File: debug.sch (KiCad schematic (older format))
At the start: 23 parts, among them J102 10118194-0001LF, J401 Conn_01x11, J402 Conn_ARM_JTAG_SWD_10, J403 FTDI_TTL_Cable, SW401 PTS810, U103 CP2102N-A02-GQFN28R

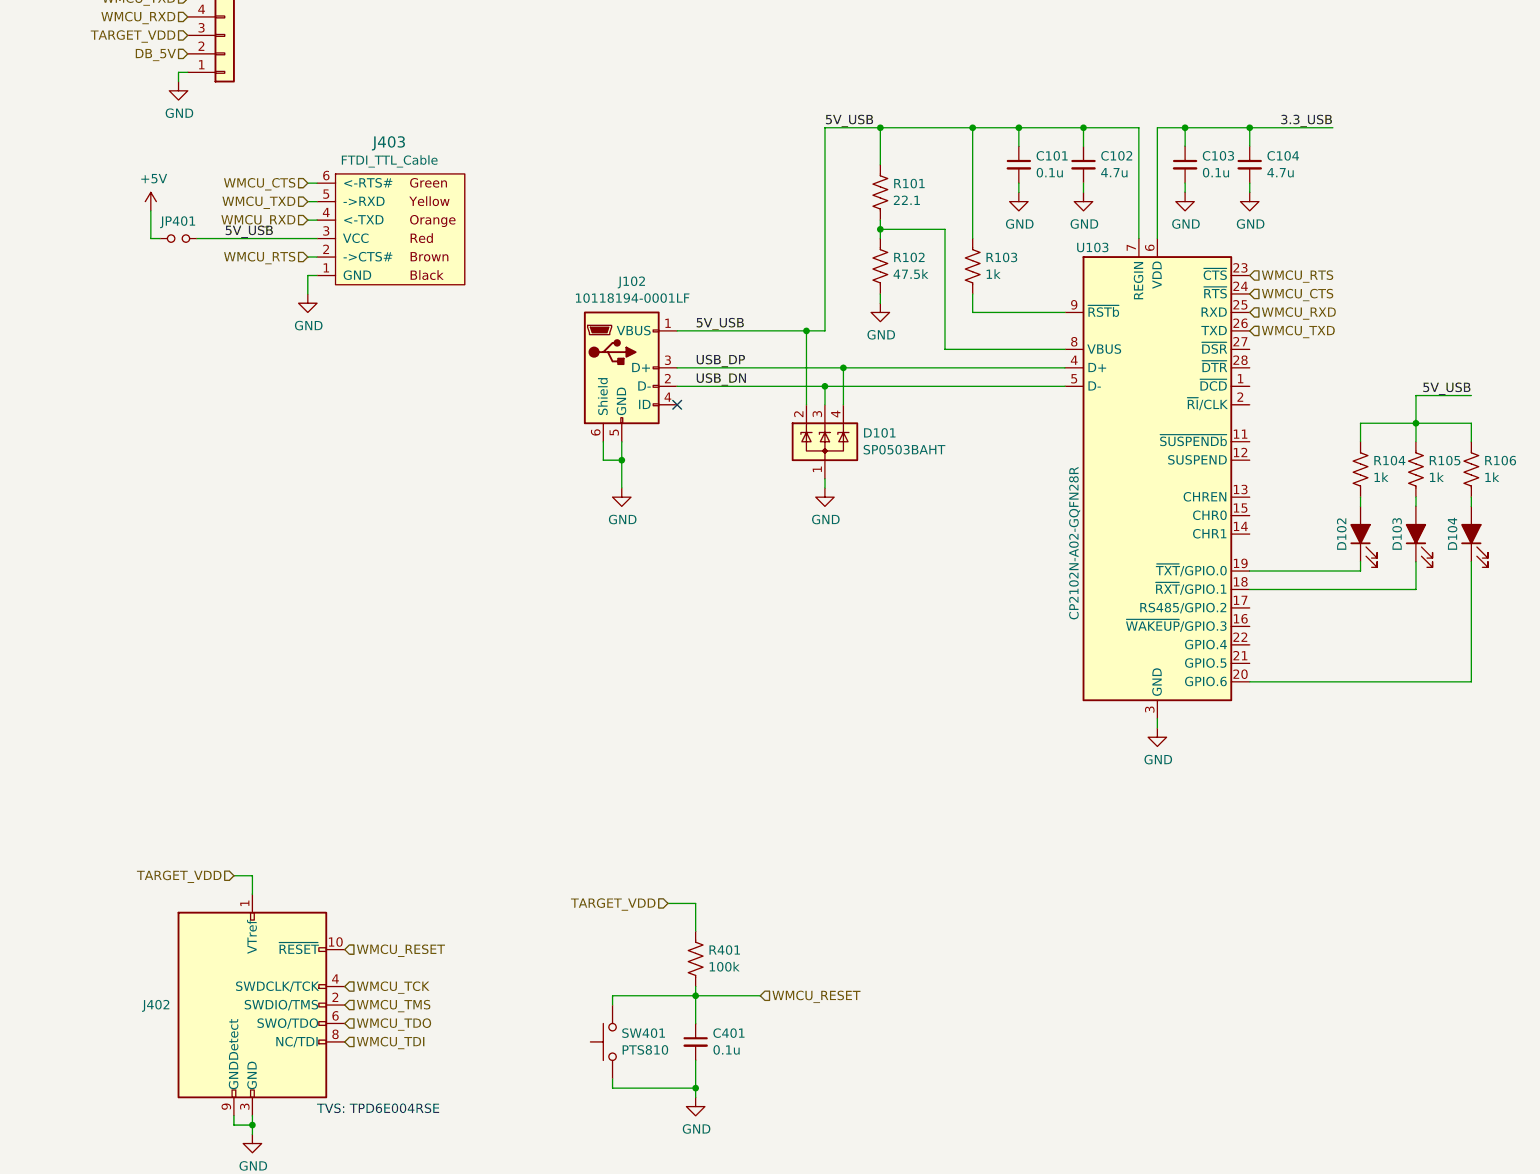
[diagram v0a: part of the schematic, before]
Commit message: Re-annotate all parts
Cleans up annotations
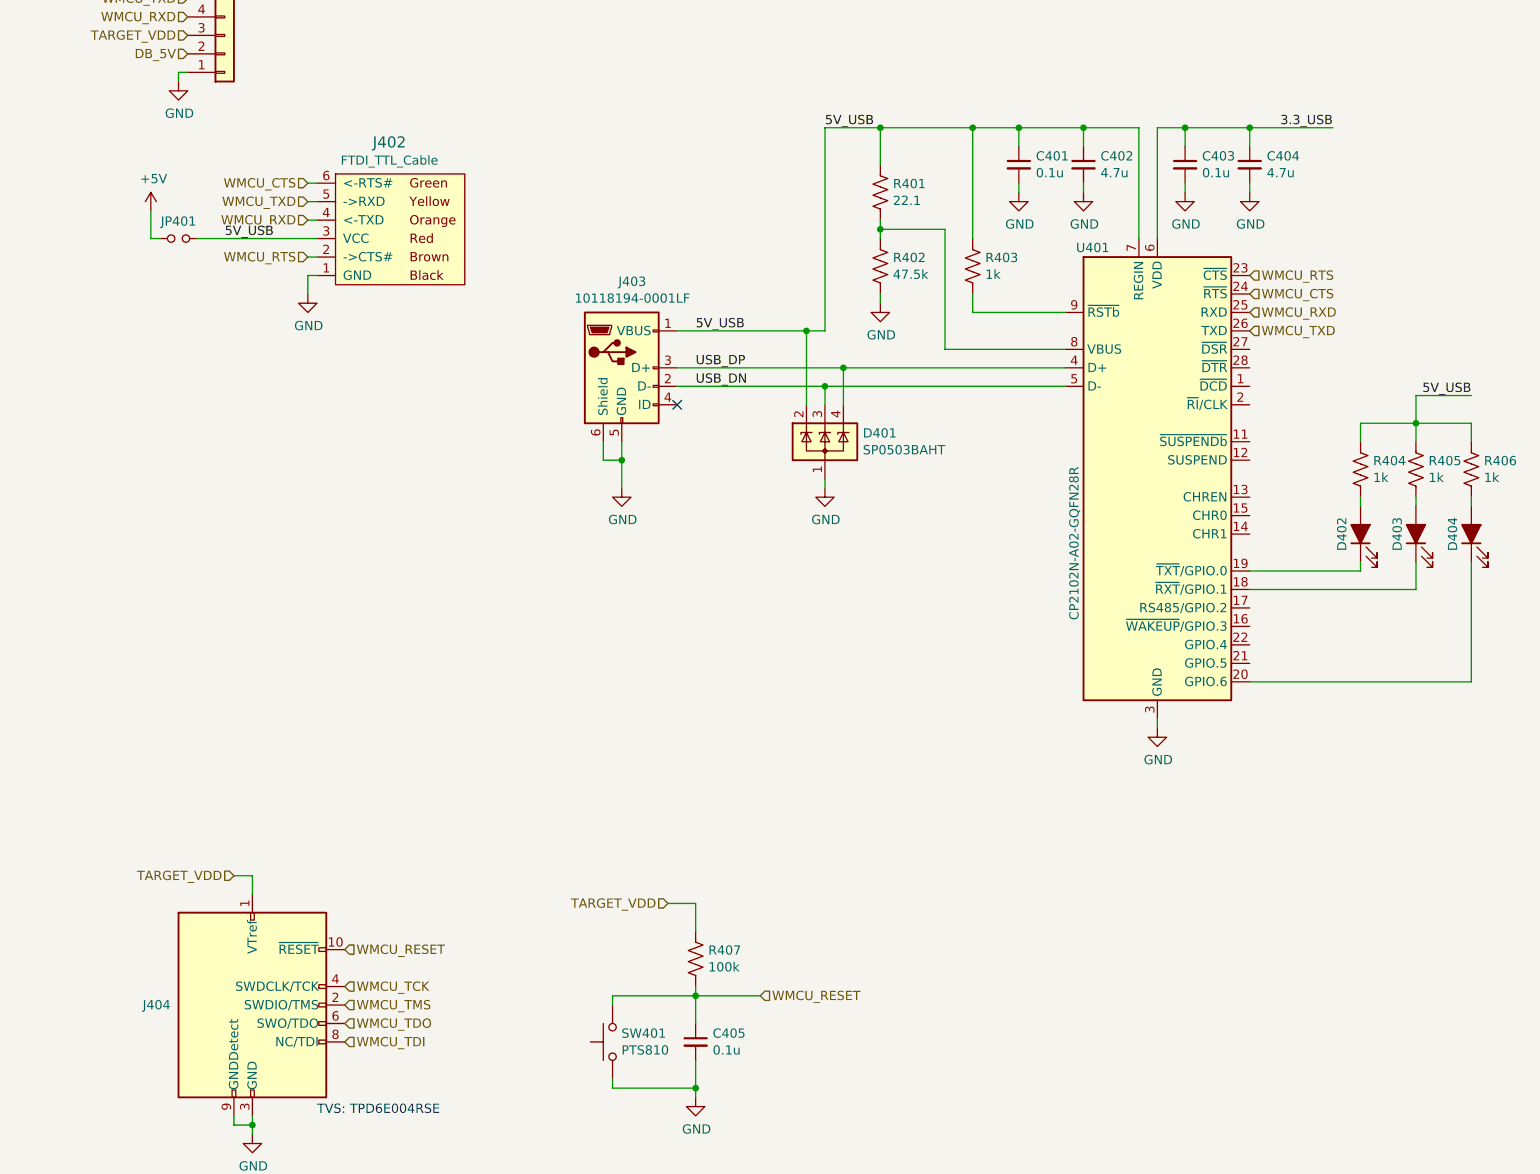
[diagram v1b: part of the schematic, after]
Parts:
- renumbered C101 to C401, C102 to C402, C103 to C403, C104 to C404, C401 to C405, D101 to D401, D102 to D402, D103 to D403, D104 to D404, J403 to J402, J102 to J403, J402 to J404, R101 to R401, R102 to R402, R103 to R403, R104 to R404, R105 to R405, R106 to R406, R401 to R407, U103 to U401

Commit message: BOM reduction and part picking
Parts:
- J402: LCSC (none) -> C190819
- R401: Digikey (none) -> 311-22.1HRCT-ND; LCSC (none) -> C137767; MPN (none) -> RC0603FR-0722R1L; Note (none) -> RES SMD 22.1 OHM 1% 1/10W 0603
- R402: Digikey (none) -> 311-47.5KHRCT-ND; LCSC (none) -> C137715; MPN (none) -> RC0603FR-0747K5L; Note (none) -> RES SMD 47.5K OHM 1% 1/10W 0603
- R403, R404, R405, R406: LCSC (none) -> C125933
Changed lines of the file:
@@
 F 2 "Connector_PinHeader_2.54mm:PinHeader_1x06_P2.54mm_Vertical" V 2250 2550 60  0001 C CNN
 F 3 "" V 1975 2725 60  0001 C CNN
+F 4 "C190819" H 2250 2650 50  0001 C CNN "LCSC"
 	1    2250 2650
 	1    0    0    1
@@
 F 5 "311-1.00KHRCT-ND" H 8100 3950 50  0001 C CNN "Digikey"
 F 6 "RES SMD 1K OHM 1% 1/10W 0603" H 8100 3950 50  0001 C CNN "Note"
+F 7 "C125933" H 8100 3950 50  0001 C CNN "LCSC"
 	1    8100 3950
 	-1   0    0    1
@@
 F 5 "311-1.00KHRCT-ND" H 7800 3950 50  0001 C CNN "Digikey"
 F 6 "RES SMD 1K OHM 1% 1/10W 0603" H 7800 3950 50  0001 C CNN "Note"
+F 7 "C125933" H 7800 3950 50  0001 C CNN "LCSC"
 	1    7800 3950
 	-1   0    0    1
@@
 F 5 "311-1.00KHRCT-ND" H 7500 3950 50  0001 C CNN "Digikey"
 F 6 "RES SMD 1K OHM 1% 1/10W 0603" H 7500 3950 50  0001 C CNN "Note"
+F 7 "C125933" H 7500 3950 50  0001 C CNN "LCSC"
 	1    7500 3950
 	-1   0    0    1
@@
 F 5 "311-1.00KHRCT-ND" H 5400 2850 50  0001 C CNN "Digikey"
 F 6 "RES SMD 1K OHM 1% 1/10W 0603" H 5400 2850 50  0001 C CNN "Note"
+F 7 "C125933" H 5400 2850 50  0001 C CNN "LCSC"
 	1    5400 2850
 	-1   0    0    1
@@
 F 2 "Resistor_SMD:R_0603_1608Metric" H 4900 2850 60  0001 C CNN
 F 3 "" H 4900 2850 60  0001 C CNN
+F 4 "311-47.5KHRCT-ND" H 4900 2850 50  0001 C CNN "Digikey"
+F 5 " C137715 " H 4900 2850 50  0001 C CNN "LCSC"
+F 6 "RC0603FR-0747K5L" H 4900 2850 50  0001 C CNN "MPN"
+F 7 "RES SMD 47.5K OHM 1% 1/10W 0603" H 4900 2850 50  0001 C CNN "Note"
 	1    4900 2850
 	-1   0    0    1
@@
 F 2 "Resistor_SMD:R_0603_1608Metric" H 4900 2450 60  0001 C CNN
 F 3 "" H 4900 2450 60  0001 C CNN
+F 4 "311-22.1HRCT-ND" H 4900 2450 50  0001 C CNN "Digikey"
+F 5 "C137767 " H 4900 2450 50  0001 C CNN "LCSC"
+F 6 "RC0603FR-0722R1L" H 4900 2450 50  0001 C CNN "MPN"
+F 7 "RES SMD 22.1 OHM 1% 1/10W 0603" H 4900 2450 50  0001 C CNN "Note"
 	1    4900 2450
 	-1   0    0    1

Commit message: Prep for gerber export
Update fields
Align standoff holes
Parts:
- U401: Manufacturer (none) -> Silicon Labs
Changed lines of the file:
@@
 F 7 "C428937" H 6400 4000 50  0001 C CNN "LCSC"
 F 8 "CP2102N-A02-GQFN28R" H 6400 4000 50  0001 C CNN "Alt"
+F 9 "Silicon Labs" H 6400 4000 50  0001 C CNN "Manufacturer"
 	1    6400 4000
 	1    0    0    -1

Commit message: Increase clearance for SWD connector
Alternatives are:
FTSH-105-01-L-DV-K
BXIDM03
3221-10-0300-00
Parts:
- J404: footprint mylib:PinHeader_2x05_P1.27mm_Thin_Shrouded_Vertical_SMD -> mylib:PinHeader_2x05_P1.27mm_Wide_Shrouded_Vertical_SMD; Alt (none) -> BXIDM03
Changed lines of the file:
@@
 F 0 "J404" H 1057 6850 50  0000 R CNN
 F 1 "Conn_ARM_JTAG_SWD_10" H 1057 6805 50  0001 R CNN
-F 2 "mylib:PinHeader_2x05_P1.27mm_Thin_Shrouded_Vertical_SMD" H 1500 6850 50  0001 C CNN
+F 2 "mylib:PinHeader_2x05_P1.27mm_Wide_Shrouded_Vertical_SMD" H 1500 6850 50  0001 C CNN
 F 3 "http://infocenter.arm.com/help/topic/com.arm.doc.ddi0314h/DDI0314H_coresight_components_trm.pdf" V 1150 5600 50  0001 C CNN
 F 4 "SAM8799-ND" H 1500 6850 50  0001 C CNN "Digikey"
 F 5 "FTSH-105-01-L-DV-K" H 1500 6850 50  0001 C CNN "MPN"
 F 6 "2x5 1.27mm SMD connector" H 1500 6850 50  0001 C CNN "Note"
+F 7 "BXIDM03" H 1500 6850 50  0001 C CNN "Alt"
 	1    1500 6850
 	1    0    0    -1

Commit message: Schematic field cleanup
Remove stray spaces
Cleaned up duplicate fields
Normalize: 100pF (C314 C803 C807) and 47uF  (C308 C310 C804 C805) according to r0 order
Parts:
- J403: LCSC C132563 -> C132563
- R401: LCSC C137767 -> C137767
- R402: LCSC C137715 -> C137715
- R407: Digikey 311-10.0KHRCT-ND -> 311-100KHRCT-ND; MPN 311-100KHRCT-ND -> RC0603FR-07100KL
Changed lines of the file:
@@
 F 2 "Resistor_SMD:R_0603_1608Metric" H 3900 6600 60  0001 C CNN
 F 3 "" H 3900 6600 60  0001 C CNN
-F 4 "311-100KHRCT-ND " H 3900 6600 50  0001 C CNN "MPN"
-F 5 "311-10.0KHRCT-ND" H 3900 6600 50  0001 C CNN "Digikey"
+F 4 "RC0603FR-07100KL" H 3900 6600 50  0001 C CNN "MPN"
+F 5 "311-100KHRCT-ND" H 3900 6600 50  0001 C CNN "Digikey"
 F 6 "RES SMD 100K OHM 1% 1/10W 0603" H 3900 6600 50  0001 C CNN "Note"
 	1    3900 6600
@@
 F 3 "" H 4900 2850 60  0001 C CNN
 F 4 "311-47.5KHRCT-ND" H 4900 2850 50  0001 C CNN "Digikey"
-F 5 " C137715 " H 4900 2850 50  0001 C CNN "LCSC"
+F 5 "C137715" H 4900 2850 50  0001 C CNN "LCSC"
 F 6 "RC0603FR-0747K5L" H 4900 2850 50  0001 C CNN "MPN"
 F 7 "RES SMD 47.5K OHM 1% 1/10W 0603" H 4900 2850 50  0001 C CNN "Note"
@@
 F 3 "" H 4900 2450 60  0001 C CNN
 F 4 "311-22.1HRCT-ND" H 4900 2450 50  0001 C CNN "Digikey"
-F 5 "C137767 " H 4900 2450 50  0001 C CNN "LCSC"
+F 5 "C137767" H 4900 2450 50  0001 C CNN "LCSC"
 F 6 "RC0603FR-0722R1L" H 4900 2450 50  0001 C CNN "MPN"
 F 7 "RES SMD 22.1 OHM 1% 1/10W 0603" H 4900 2450 50  0001 C CNN "Note"
@@
 F 5 "609-4618-1-ND" H 3500 3400 50  0001 C CNN "Digikey"
 F 6 "CONN RCPT USB2.0 MICRO B SMD R/A" H 3500 3400 50  0001 C CNN "Note"
-F 7 "C132563 " H 3500 3400 50  0001 C CNN "LCSC"
+F 7 "C132563" H 3500 3400 50  0001 C CNN "LCSC"
 	1    3500 3400
 	1    0    0    -1

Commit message: Add generated files
Added title block to pcb
Fixed backup lib for USB connector
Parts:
- J403: symbol SD1-rescue:USB_B_Micro-Connector -> Connector:USB_B_Micro
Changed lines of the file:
@@
 	4600 3200 4600 2100
 $Comp
-L SD1-rescue:USB_B_Micro-Connector J403
+L Connector:USB_B_Micro J403
 U 1 1 5F75B1A8
 P 3500 3400
